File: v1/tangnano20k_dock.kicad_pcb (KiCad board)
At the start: 2 copper layers, 161.9 x 73.7 mm, 84 parts, among them J1 Mini-DIN-6, J10 DB9_Male_MountingHoles, J11 DB9_Male_MountingHoles, J12 Cliff DC10A, J2 2x20 Pin Female, J3 Conn_01x03_Male, J4 Conn_01x20, J5 Conn_01x02, J6 RCA, J7 FCR684205T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

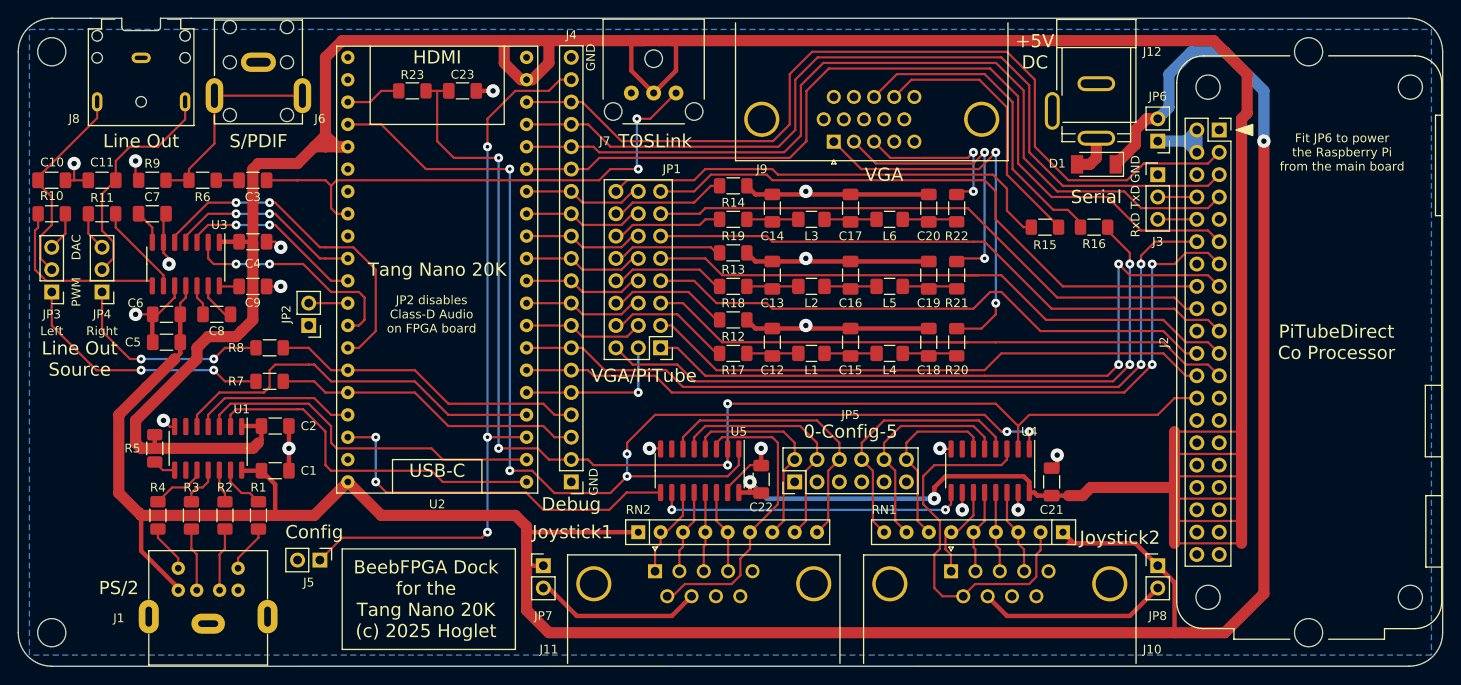
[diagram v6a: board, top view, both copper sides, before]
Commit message: Beef up longer 5V tracks
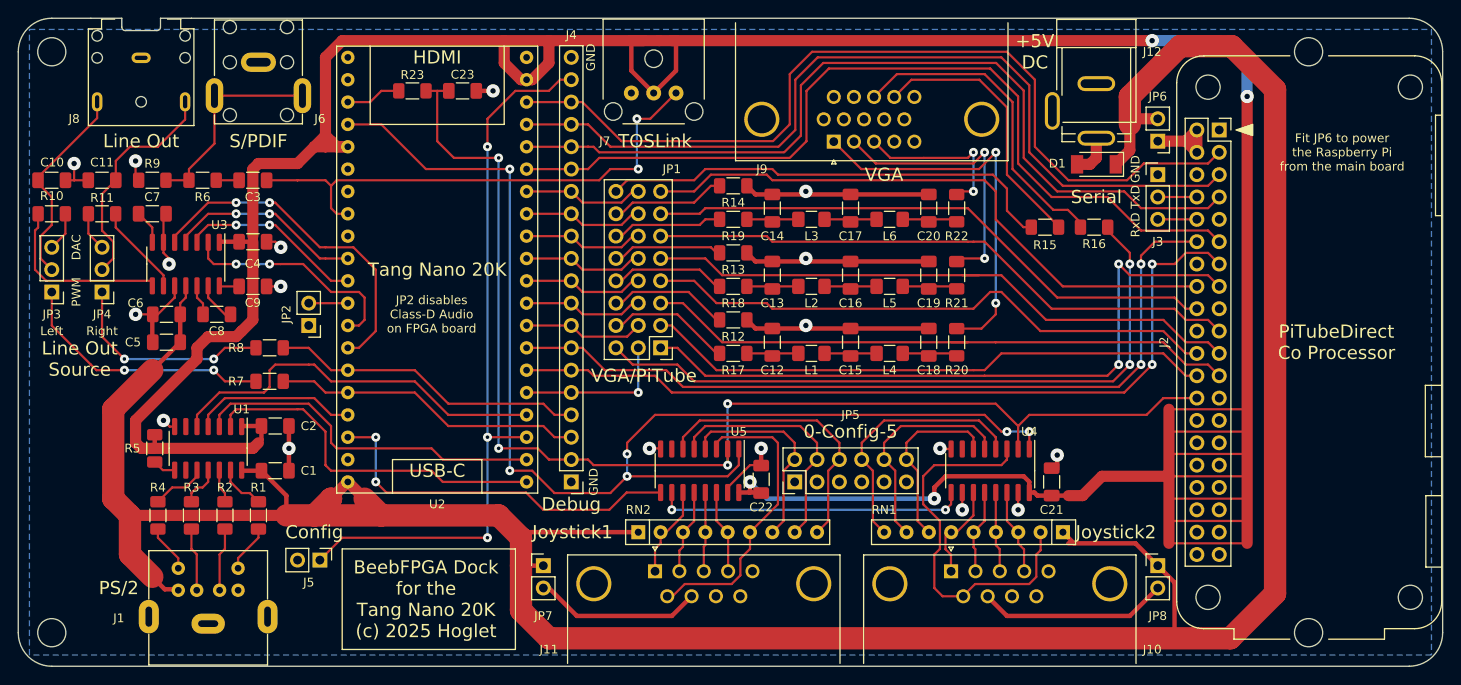
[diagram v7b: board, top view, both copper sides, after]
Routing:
- net +3.3V: track 392.1 -> 411.1 mm, vias 2 -> 4
- net +5V: track 313.0 -> 330.5 mm, vias 1 -> 0

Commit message: Silk screen
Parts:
- moved J5 8.89 mm to (107.3, 120.0)
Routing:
- net /KEY_CONF: track 83.5 -> 92.4 mm
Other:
- board text added: "BeebFPGA Dock for the Tang Nano 20K Version 1.00 (c) 2025 Hoglet"
- board text added: "Key Config"
- board text added: "VGA/Tube"
- board text added: "WARNING: Power from +5V DC Jack or Tang USB-C DO NOT USE BOTH!!!"
- board text removed: "BeebFPGA Dock for the Tang Nano 20K (c) 2025 Hoglet"
- board text removed: "Config"
- board text removed: "VGA/PiTube"
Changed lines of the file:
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@@
     (property "Sheetname" "")
     (attr through_hole)
-    (fp_text reference "J7" (at 5.56 -13.97 unlocked) (layer "F.SilkS")
+    (fp_text reference "J7" (at -7.14 -10.795 unlocked) (layer "F.SilkS")
       (effects (font (size 1 1) (thickness 0.15)))
     )
@@
     (property "Sheetname" "")
     (attr through_hole)
-    (fp_text reference "J2" (at -6.27 24.13 90) (layer "F.SilkS")
+    (fp_text reference "J2" (at -6.27 24.13 180) (layer "F.SilkS")
       (effects (font (size 1 1) (thickness 0.15)))
     )
@@
     (property "Sheetname" "")
     (attr through_hole)
-    (fp_text reference "J3" (at 0 7.62) (layer "F.SilkS")
+    (fp_text reference "J3" (at -4.445 2.54) (layer "F.SilkS")
       (effects (font (size 1 1) (thickness 0.15)))
     )
@@
   )
   (footprint "Connector_PinHeader_2.54mm:PinHeader_1x02_P2.54mm_Vertical" (layer "F.Cu")
-    (at 107.315 111.12 -90)
+    (at 107.315 120.01 -90)
     (descr "Through hole straight pin header, 1x02, 2.54mm pitch, single row")
     (tags "Through hole pin header THT 1x02 2.54mm single row")
@@
     (property "Sheetname" "")
     (attr through_hole)
-    (fp_text reference "J5" (at 2.54 1.27 180) (layer "F.SilkS")
+    (fp_text reference "J5" (at -6.985 1.27 180) (layer "F.SilkS")
       (effects (font (size 1 1) (thickness 0.15)))
     )
@@
     (property "Sheetname" "")
     (attr through_hole)
-    (fp_text reference "U2" (at 10.16 -2.535 unlocked) (layer "F.SilkS")
+    (fp_text reference "U2" (at 10.16 5.085 unlocked) (layer "F.SilkS")
       (effects (font (size 1 1) (thickness 0.15)))
     )
@@
       (effects (font (size 1 1) (thickness 0.15)))
     )
+    (fp_text user "SD Card" (at 10.16 -3.805 unlocked) (layer "F.SilkS")
+      (effects (font (size 1.5 1.5) (thickness 0.2)))
+    )
     (fp_text user "HDMI" (at 10.16 48.26 unlocked) (layer "F.SilkS")
       (effects (font (size 1.5 1.5) (thickness 0.2)))
     )
-    (fp_text user "Tang Nano 20K" (at 10.16 24.13 unlocked) (layer "F.SilkS")
+    (fp_text user "Tang Nano 20K" (at 10.16 31.755 unlocked) (layer "F.SilkS")
       (effects (font (size 1.5 1.5) (thickness 0.2)))
     )
@@
     (property "Sheetname" "VGA")
     (attr through_hole)
-    (fp_text reference "J9" (at 8.185 -3.12) (layer "F.SilkS")
+    (fp_text reference "J9" (at -20.955 -1.215) (layer "F.SilkS")
       (effects (font (size 1 1) (thickness 0.15)))
     )
@@
     (property "Sheetname" "")
     (attr through_hole)
-    (fp_text reference "JP1" (at -1.27 20.32) (layer "F.SilkS")
+    (fp_text reference "JP1" (at 0.635 20.32) (layer "F.SilkS")
       (effects (font (size 1 1) (thickness 0.15)))
     )
@@
     (property "Sheetname" "")
     (attr through_hole)
-    (fp_text reference "J1" (at 10.16 -3.175 unlocked) (layer "F.SilkS")
+    (fp_text reference "J1" (at 8.89 -6.731 unlocked) (layer "F.SilkS")
       (effects (font (size 1 1) (thickness 0.15)))
     )
@@
     (effects (font (size 1.5 1.5) (thickness 0.2)))
   )
-  (gr_text "Config" (at 106.68 107.945) (layer "F.SilkS")
-    (effects (font (size 1.5 1.5) (thickness 0.2)))
+  (gr_text "Key\nConfig" (at 106.045 116.2) (layer "F.SilkS")
+    (effects (font (size 1.2 1.2) (thickness 0.2)))
   )
   (gr_text "Debug" (at 135.89 104.77) (layer "F.SilkS")
@@
     (effects (font (size 1 1) (thickness 0.15)))
   )
-  (gr_text "Serial" (at 195.58 69.845) (layer "F.SilkS")
+  (gr_text "Serial" (at 201.295 75.56) (layer "F.SilkS")
     (effects (font (size 1.5 1.5) (thickness 0.2)))
   )
@@
     (effects (font (size 1 1) (thickness 0.15)))
   )
-  (gr_text "VGA/PiTube" (at 144.145 90.165) (layer "F.SilkS")
+  (gr_text "VGA/Tube" (at 143.51 90.165) (layer "F.SilkS")
     (effects (font (size 1.5 1.5) (thickness 0.2)))
   )
@@
     (effects (font (size 1.5 1.5) (thickness 0.2)))
   )
-  (gr_text "BeebFPGA Dock\nfor the\nTang Nano 20K\n(c) 2025 Hoglet" (at 119.38 115.565) (layer "F.SilkS")
-    (effects (font (size 1.5 1.5) (thickness 0.2)))
+  (gr_text "BeebFPGA Dock\nfor the\nTang Nano 20K\nVersion 1.00\n(c) 2025 Hoglet\n" (at 119.38 115.565) (layer "F.SilkS")
+    (effects (font (size 1.2 1.2) (thickness 0.15)))
   )
   (gr_text "GND" (at 138.1125 53.97 90) (layer "F.SilkS")
@@
     (effects (font (size 1.5 1.5) (thickness 0.2)) (justify left))
   )
-  (gr_text "JP2 disables\nClass-D Audio\non FPGA board" (at 120.015 83.18) (layer "F.SilkS")
+  (gr_text "JP2 disables\nClass-D Audio\non FPGA board" (at 80.645 93.975) (layer "F.SilkS")
     (effects (font (size 1 1) (thickness 0.15)))
   )
@@
     (effects (font (size 1.5 1.5) (thickness 0.2)))
   )
-  (gr_text "PS/2" (at 84.455 114.295) (layer "F.SilkS")
+  (gr_text "PS/2" (at 84.455 112.39) (layer "F.SilkS")
     (effects (font (size 1.5 1.5) (thickness 0.2)))
   )
@@
     (effects (font (size 1.5 1.5) (thickness 0.2)))
   )
-  (gr_text "VGA" (at 171.45 67.305) (layer "F.SilkS")
+  (gr_text "VGA" (at 170.18 67.305) (layer "F.SilkS")
     (effects (font (size 1.5 1.5) (thickness 0.2)))
   )
@@
     (effects (font (size 1 1) (thickness 0.15)))
   )
+  (gr_text "WARNING:\n\nPower from\n+5V DC Jack\nor\nTang USB-C\n\nDO NOT\nUSE BOTH!!!" (at 120.65 82.545) (layer "F.SilkS")
+    (effects (font (size 1.2 1.2) (thickness 0.15)))
+  )
   (segment (start 177.865 98.49) (end 179.07 98.49) (width 0.254) (layer "F.Cu") (net 1))
   (segment (start 144.8125 98.425) (end 146.0175 98.425) (width 0.254) (layer "F.Cu") (net 1))
@@
   (segment (start 132.715 114.295) (end 133.35 114.295) (width 0.508) (layer "F.Cu") (net 135))
   (segment (start 129.54 57.78) (end 133.35 57.78) (width 0.254) (layer "F.Cu") (net 137))
-  (segment (start 133.35 57.78) (end 134.62 56.51) (width 0.254) (layer "F.Cu") (net 137))
   (segment (start 109.855 108.58) (end 107.315 111.12) (width 0.254) (layer "F.Cu") (net 137))
+  (segment (start 107.315 111.12) (end 107.315 120.01) (width 0.254) (layer "F.Cu") (net 137))
+  (segment (start 133.35 57.78) (end 134.62 56.51) (width 0.254) (layer "F.Cu") (net 137))
   (segment (start 126.365 97.15) (end 130.805 97.15) (width 0.254) (layer "F.Cu") (net 137))
   (segment (start 126.365 64.13) (end 126.365 60.955) (width 0.254) (layer "F.Cu") (net 137))
